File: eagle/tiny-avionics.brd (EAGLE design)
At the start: 65.8 x 25.4 mm, 67 parts, among them J1 USB-MICROB, J3 JST-PH-2-SMT-RA, U1 LP5907, U2 M25P10-AVMN6TP_TR, U3 LSM9DS0, U5 LTC1998, U6 ATMEGA32U4-AU, X1 8MHz

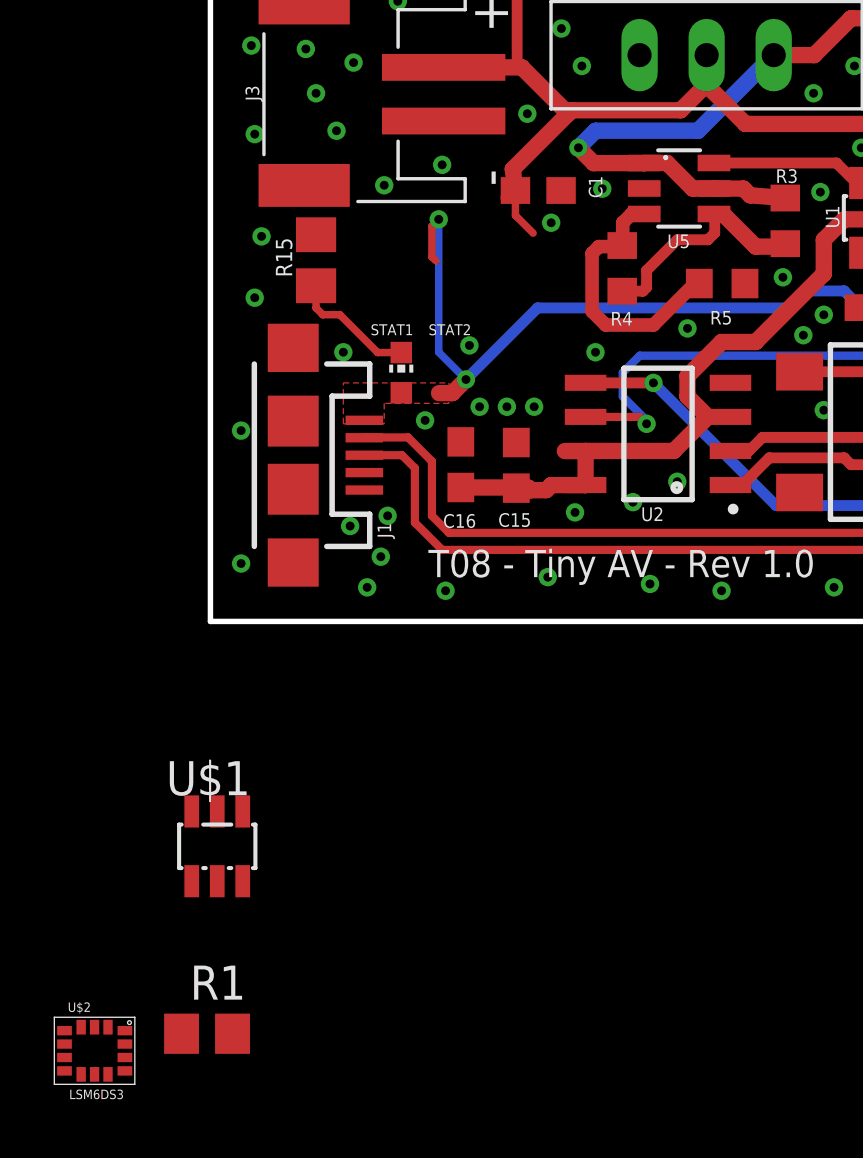
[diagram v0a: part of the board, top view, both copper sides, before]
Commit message: Reverted board files on master to known-good version
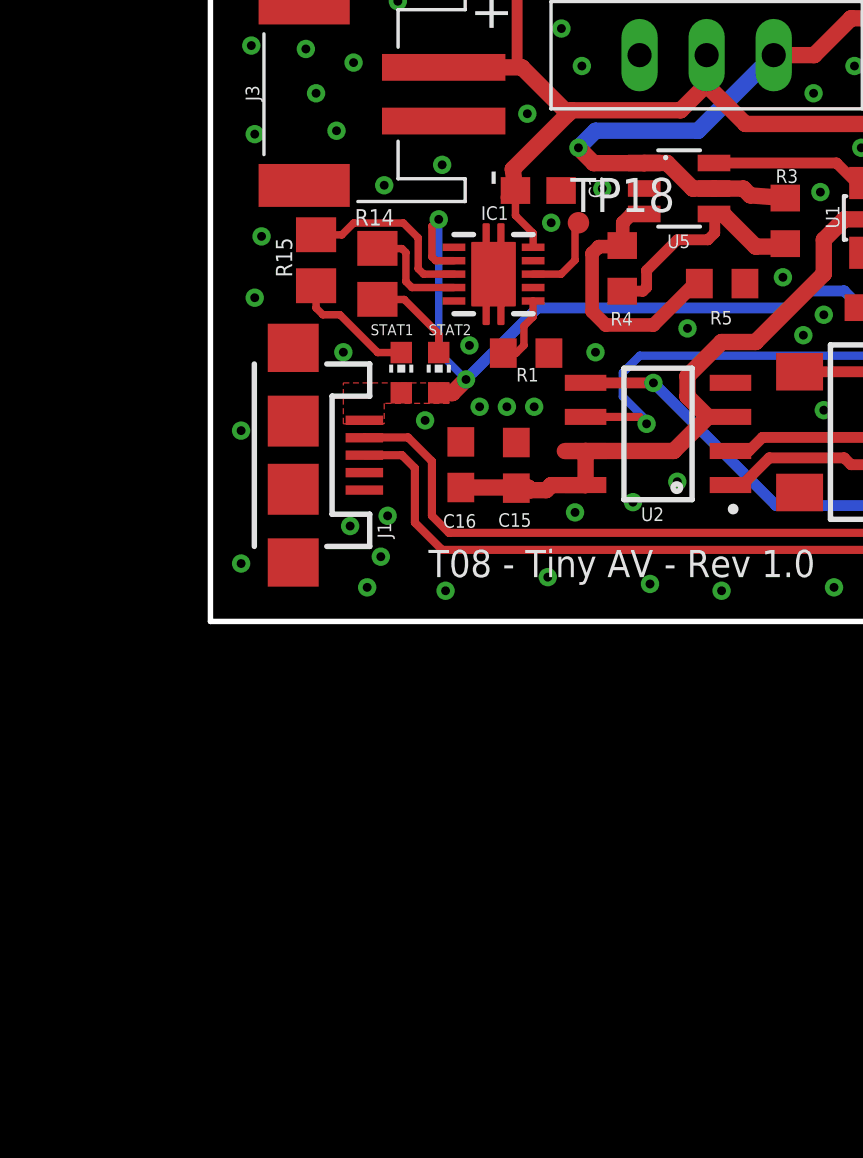
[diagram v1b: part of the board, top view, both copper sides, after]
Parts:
- removed U$1: BQ21040, tinyav-lib:SOT23-6L
- removed U$2: LSM6DS3, tinyav-lib:LGA-14L
- added IC1: BQ24022, tinyav-lib:DRC-S-PVSON-N10
- added LED3: (no value), adafruit:CHIP-LED0603
- added R14: 330, rcl:R0805
- added TP18: TPTP08R, testpad:TP08R
- R1: value 5.36k -> 4k; device rcl:R0805 -> rcl:R0603
- R15, R16, R6, R7, R8: value 3.3k -> 330
- moved R1 28.0 mm to (11.8, 10.0), turned to 180 degrees
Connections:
- new net N$50: IC1.3, R15.2
- new net N$51: IC1.4, R14.2
- new net N$68: IC1.8, TP18.TP
- net GND: now also IC1.5, IC1.7, IC1.9; no longer U$1.5
- net N$13: now also IC1.10; no longer U$1.2
- net N$4: now also IC1.6, R1.2; no longer R15.2, U$1.3
- net N$49: now also LED3.C, R14.1; no longer R1.2, U$1.4
- net VBUS1: now also IC1.2, LED3.A; no longer U$1.6
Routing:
- net N$50: track 0.00 -> 6.79 mm
- net N$51: track 0.00 -> 4.10 mm
- net N$49: track 0.00 -> 3.51 mm
- net N$68: track 0.00 -> 3.23 mm
- net N$4: track 0.00 -> 2.69 mm
- net VBUS1: track 62.1 -> 62.8 mm
- net N$13: track 35.1 -> 35.7 mm

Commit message: Merge commit to overwrite eagle files
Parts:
- removed C4: .22µ, rcl:C0603
- removed C9: 2.2µ, rcl:C0603
- removed IC1: BQ24022, tinyav-lib:DRC-S-PVSON-N10
- removed LED3: (no value), adafruit:CHIP-LED0603
- removed R14: 330, rcl:R0805
- removed R9: 0, rcl:R0603
- removed TP16, TP17, TP18: TPTP08R, testpad:TP08R
- added U$1: 10k B25/50=3375k, tinyav-lib:R0603
- added U4: BQ21040, tinyav-lib:SOT23-6L
- C2: device rcl:C0805 -> rcl:C0603
- C3: value 4.7µ -> 2.2µ
- R1: value 4k -> 5.36k
- R15, R16, R6, R7, R8: value 330 -> 3.3k; device rcl:R0805 -> rcl:R0603
- R2: device rcl:R0805 -> rcl:R0603
- U2: value M25P10-AVMN6TP_TR -> M25PX16; device SOIC127P600X175-8N:SOIC127P600X175-8N -> tinyav-lib:SO8
- U3: value LSM9DS0 -> LSM6DS3; device LSM9DS0:LGA-24 -> tinyav-lib:LGA-14L
- X1: device IQD-Frequency-Products:HC49 -> tinyav-lib:ATS-SM
- moved TP14 49.5 mm to (1.78, 13.1)
- moved C2 45.0 mm to (4.00, 12.9), turned to 90 degrees
- moved LED4 41.4 mm to (26.0, 22.5), turned to 0 degrees
- moved R16 40.6 mm to (23.9, 22.5), turned to 270 degrees
- moved C3 36.2 mm to (22.9, 14.6), turned to 0 degrees
- moved JP2 34.2 mm to (29.5, 6.73), turned to 180 degrees
- moved S2 29.3 mm to (55.4, 6.42), turned to 270 degrees
- moved U3 27.8 mm to (27.8, 13.0)
- moved TP15 26.0 mm to (21.7, 19.1)
- moved C5 22.0 mm to (26.2, 16.8)
- moved R2 21.9 mm to (55.5, 11.5), turned to 90 degrees
- moved C6 21.8 mm to (27.9, 16.7)
- moved R7 20.5 mm to (52.8, 15.9), turned to 0 degrees
- moved C7 18.6 mm to (48.0, 19.4), turned to 90 degrees
- moved R6 17.9 mm to (52.8, 14.1)
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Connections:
- net N$52 renamed TP3
- net N$54 renamed TP12
- net N$55 renamed TP11
- net N$56 renamed TP10
- net N$57 renamed TP9
- net N$58 renamed TP8
- net N$59 renamed TP7
- net N$60 renamed TP1
- net N$61 renamed TP2
- net N$62 renamed TP4
- net N$63 renamed TP5
- net N$64 renamed TP6
- removed net GYR_EN: R9.1, U3.19
- removed net N$16: U3.14, U6.20
- removed net N$17: U3.13, U6.19
- removed net N$19: U3.11, U6.18
- removed net N$20: R9.2, U6.38
- removed net N$50: IC1.3, R15.2
- removed net N$51: IC1.4, R14.2
- removed net N$66: TP17.TP, U3.10
- removed net N$67: TP16.TP, U3.12
- removed net N$68: IC1.8, TP18.TP
- net CLK: now also U3.13; no longer U3.21
- net GND: now also C3.2, U$1.2, U3.7, U4.5; no longer C3.1, C9.2, IC1.5, IC1.7, IC1.9, U3.4, U3.5
- net MISO: now also U3.1; no longer U3.22, U3.23
- net MOSI: now also U3.14; no longer U3.24
- net N$10: now also U3.4, U6.18; no longer C4.2, U3.8
- net N$11: now also U6.19; no longer C4.1
- net N$13: now also U4.2; no longer IC1.10
- net N$4: now also R15.2, U4.3; no longer IC1.6, R1.2
- net N$49: now also R1.2, U4.4; no longer LED3.C, R14.1
- net N$9: now also U$1.1, U4.1; no longer C3.2, U3.7
- net VBUS1: now also U4.6; no longer IC1.2, LED3.A
- net VCC: now also C3.1, U3.5, U3.8; no longer C9.1, U3.15, U3.16, U3.17, U3.18
- net XM_EN: now also U3.12; no longer U3.20
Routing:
- net MOSI: track 73.6 -> 30.2 mm, vias 3 -> 2
- net N$3: track 95.2 -> 54.2 mm
- net MISO: track 64.2 -> 25.6 mm, vias 3 -> 2
- net MEM_EN: track 16.1 -> 54.2 mm
- net GYR_EN: track 28.1 -> 0.00 mm, vias 2 -> 0
- net CLK: track 75.1 -> 49.9 mm, vias 3 -> 0
- net N$10: track 2.88 -> 25.4 mm, vias 0 -> 2
- net N$11: track 1.77 -> 22.6 mm, vias 0 -> 2
- net N$17: track 18.6 -> 0.00 mm, vias 2 -> 0
- net N$16: track 18.4 -> 0.00 mm, vias 2 -> 0
- net N$19: track 14.6 -> 0.00 mm, vias 2 -> 0
- net FIRE_EN: track 32.1 -> 18.4 mm, vias 3 -> 1
- net N$9: track 2.46 -> 15.9 mm, vias 0 -> 1
- net N$65: track 2.78 -> 16.1 mm, vias 0 -> 2
- net N$1: track 13.6 -> 1.83 mm, vias 2 -> 0
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- removed copper zone on layer 1, net VBUS1
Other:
- board size 65.8 x 25.4 mm -> 61.7 x 25.4 mm
- board text added: "CHG"
- board text added: "FIRE"
- board text added: "GND"
- board text added: "OFF"
- board text added: "ON"
- board text added: "POWER ON"
- board text added: "Tiny Avionics - Rev 2.0"
- board text removed: "Power"
- board text removed: "STAT1"
- board text removed: "STAT2"
- board text removed: "T08 - Tiny AV - Rev 1.0"
- board text removed: "VBAT"
- board text removed: "VBUS"
